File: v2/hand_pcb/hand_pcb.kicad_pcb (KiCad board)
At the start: 2 copper layers, 70 x 96.4 mm, 72 parts, among them J1 Screw_Terminal_01x10, J10 8P8C, J2 Conn_01x08, J3 Conn_01x08, J4 Conn_01x02, J5 Conn_01x02, J6 Conn_01x08, J7 Conn_01x03, J9 Conn_02x02_Top_Bottom, M1 Motor_Servo_FB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

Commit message: Doing some things
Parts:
- removed R26, R27, R28, R29: 0R, Resistor_THT:R_Axial_DIN0207_L6.3mm_D2.5mm_P10.16mm_Horizontal
- D1, D2, D3, D4, D5: value 1N5819 -> SB5100-T; footprint Diode_THT:D_DO-41_SOD81_P10.16mm_Horizontal -> Diode_THT:D_DO-201AD_P12.70mm_Horizontal
- U4, U5: value ADS7830 -> ~; footprint Package_SO:TSSOP-16_4.4x5mm_P0.65mm -> Package_DFN_QFN:WQFN-16-1EP_3x3mm_P0.5mm_EP1.68x1.68mm
- moved R7 169.2 mm to (26.8, 41.3), turned to 0 degrees
- moved R6 156.0 mm to (26.8, 37.3), turned to 0 degrees
- moved R5 143.1 mm to (26.8, 33.2), turned to 0 degrees
- moved H4 135.3 mm to (70.8, 66.1)
- moved R2 132.8 mm to (26.8, 21.1), turned to 0 degrees
- moved H2 129.8 mm to (70.8, 50.2)
- moved R1 121.2 mm to (26.8, 17.0), turned to 0 degrees
- moved H3 84.7 mm to (70.8, 58.2)
- moved J6 72.5 mm to (100.0, 17.3)
- moved H1 67.6 mm to (70.8, 42.3)
- moved R25 67.2 mm to (26.8, 81.8)
- moved U1 52.5 mm to (191.7, 81.4), turned to 90 degrees
- moved U5 41.4 mm to (210.8, 78.0), turned to 0 degrees
- moved J5 40.3 mm to (148.4, 114.8)
- moved C1 38.8 mm to (87.9, 62.5)
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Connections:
- R22 pad 1: Net-(U4-A0) -> Net-(U4-DECAP)
- R22 pad 2: +5V -> Net-(U4-ADDR)
- R23 pad 1: Net-(U4-A0) -> Net-(U4-ADDR)
- R24 pad 1: GND -> Net-(U5-DECAP)
- R24 pad 2: Net-(U4-A1) -> Net-(U5-ADDR)
- R25 pad 1: +5V -> Net-(U5-ADDR)
- R25 pad 2: Net-(U4-A1) -> GND
- U4 pad 1: SERVO_FB_8 -> SERVO_FB_6
- U4 pad 11: GND -> Net-(U4-ADDR)
- U4 pad 12: Net-(U4-A0) -> unconnected-(U4-ALERT-Pad12)
- U4 pad 13: Net-(U4-A1) -> SCL
- U4 pad 14: SCL -> SDA
- U4 pad 15: SDA -> SERVO_FB_8
- U4 pad 16: +5V -> SERVO_FB_7
- U4 pad 2: SERVO_FB_7 -> SERVO_FB_5
- U4 pad 3: SERVO_FB_6 -> SERVO_FB_4
- U4 pad 4: SERVO_FB_5 -> SERVO_FB_3
- U4 pad 5: SERVO_FB_4 -> SERVO_FB_2
- U4 pad 6: SERVO_FB_3 -> SERVO_FB_1
- U4 pad 7: SERVO_FB_2 -> +5V
- U4 pad 8: SERVO_FB_1 -> Net-(U4-DECAP)
- U5 pad 1: SERVO_FB_10 -> unconnected-(U5-AIN2-Pad1)
- U5 pad 11: GND -> Net-(U5-ADDR)
- U5 pad 12: Net-(U5-A0) -> unconnected-(U5-ALERT-Pad12)
- U5 pad 13: Net-(U5-A1) -> SCL
- U5 pad 14: SCL -> SDA
- U5 pad 15: SDA -> SERVO_FB_10
- U5 pad 16: +5V -> SERVO_FB_9
- U5 pad 2: SERVO_FB_9 -> unconnected-(U5-AIN3-Pad2)
- U5 pad 7: unconnected-(U5-CH6-Pad7) -> +5V
- U5 pad 8: unconnected-(U5-CH7-Pad8) -> Net-(U5-DECAP)
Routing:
- net +12V: track 47.9 -> 0.00 mm
- net SERVO_FB_8: track 0.00 -> 39.2 mm
- net SERVO_FB_7: track 0.00 -> 32.0 mm
- net SERVO_FB_6: track 0.00 -> 25.8 mm
- net SERVO_FB_5: track 0.00 -> 19.3 mm
- net DSCL+: track 0.00 -> 18.0 mm
- net DSDA-: track 3.18 -> 19.8 mm
- net SERVO_FB_4: track 0.00 -> 12.9 mm
- net DSCL-: track 0.00 -> 12.1 mm
- net SERVO_FB_1: track 0.00 -> 10.7 mm
- net DSDA+: track 3.18 -> 10.6 mm
- net Net-(D3-A): track 24.1 -> 16.9 mm
- net Net-(D4-A): track 24.1 -> 17.0 mm
- net SERVO_FB_3: track 0.00 -> 6.42 mm
- net Net-(D2-A): track 24.2 -> 17.9 mm
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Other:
- board outline removed

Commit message: Doing more things
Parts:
- removed J2, J3, J6: Conn_01x08, Connector_PinHeader_2.54mm:PinHeader_1x08_P2.54mm_Vertical
- moved R10 190.5 mm to (206.0, 118.1), turned to 90 degrees
- moved R24 188.4 mm to (215.0, 87.1), turned to 90 degrees
- moved R25 188.3 mm to (215.0, 89.9), turned to -90 degrees
- moved R7 186.4 mm to (210.5, 73.2), turned to 90 degrees
- moved R8 175.7 mm to (197.0, 89.0), turned to -90 degrees
- moved R6 173.4 mm to (196.5, 73.2), turned to 90 degrees
- moved R9 171.8 mm to (194.0, 89.0), turned to -90 degrees
- moved R5 160.6 mm to (182.5, 72.7), turned to 90 degrees
- moved R4 159.3 mm to (160.0, 116.6), turned to 90 degrees
- moved R3 158.7 mm to (156.5, 116.6), turned to 90 degrees
- moved H2 156.2 mm to (213.0, 115.0)
- moved R2 150.8 mm to (168.5, 72.7), turned to 90 degrees
- moved H3 143.4 mm to (213.0, 39.0)
- moved R1 139.2 mm to (154.5, 72.6), turned to 90 degrees
- moved R11 134.7 mm to (156.5, 93.9), turned to -90 degrees
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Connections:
- J9 pad 3: +5V -> +12V
- J9 pad 4: +12V -> +5V
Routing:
- net +12V: track 0.00 -> 173.6 mm, vias 0 -> 9
- net SDA: track 0.00 -> 113.9 mm, vias 0 -> 4
- net SCL: track 0.00 -> 109.7 mm, vias 0 -> 5
- net Net-(U2-GPA4): track 0.00 -> 58.0 mm, vias 0 -> 6
- net Net-(J2-Pin_1): track 2.02 -> 57.3 mm
- net Net-(J2-Pin_2): track 2.56 -> 52.9 mm
- net Net-(U2-GPA3): track 0.00 -> 46.8 mm, vias 0 -> 2
- net Net-(J2-Pin_3): track 2.10 -> 45.9 mm
- net Net-(U2-GPA0): track 0.00 -> 38.0 mm, vias 0 -> 3
- net Net-(U2-GPA2): track 0.00 -> 36.3 mm, vias 0 -> 3
- net Net-(J2-Pin_4): track 2.64 -> 37.5 mm
- net LIMIT_SW_R: track 0.00 -> 31.8 mm
- net Net-(J3-Pin_5): track 0.00 -> 31.1 mm, vias 0 -> 3
- net +5V: track 0.00 -> 30.9 mm, vias 0 -> 3
- net Net-(J2-Pin_5): track 2.19 -> 32.5 mm
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- added copper zone on B.Cu, net +12V
- added copper zone on F.Cu, net +5V
- added copper zone on B.Cu, net GND
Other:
- board outline added: 70 x 85 mm
- board text added: "+"
- board text added: "-"
- board text added: "BOT-HOVEN"
- board text added: "DESIGNED BY"
- board text added: "GND"
- board text added: "HAND PCB"
- board text added: "J. PETERSEN"
- board text added: "SCL"
- board text added: "SDA"
- board text added: "VERSION 2"

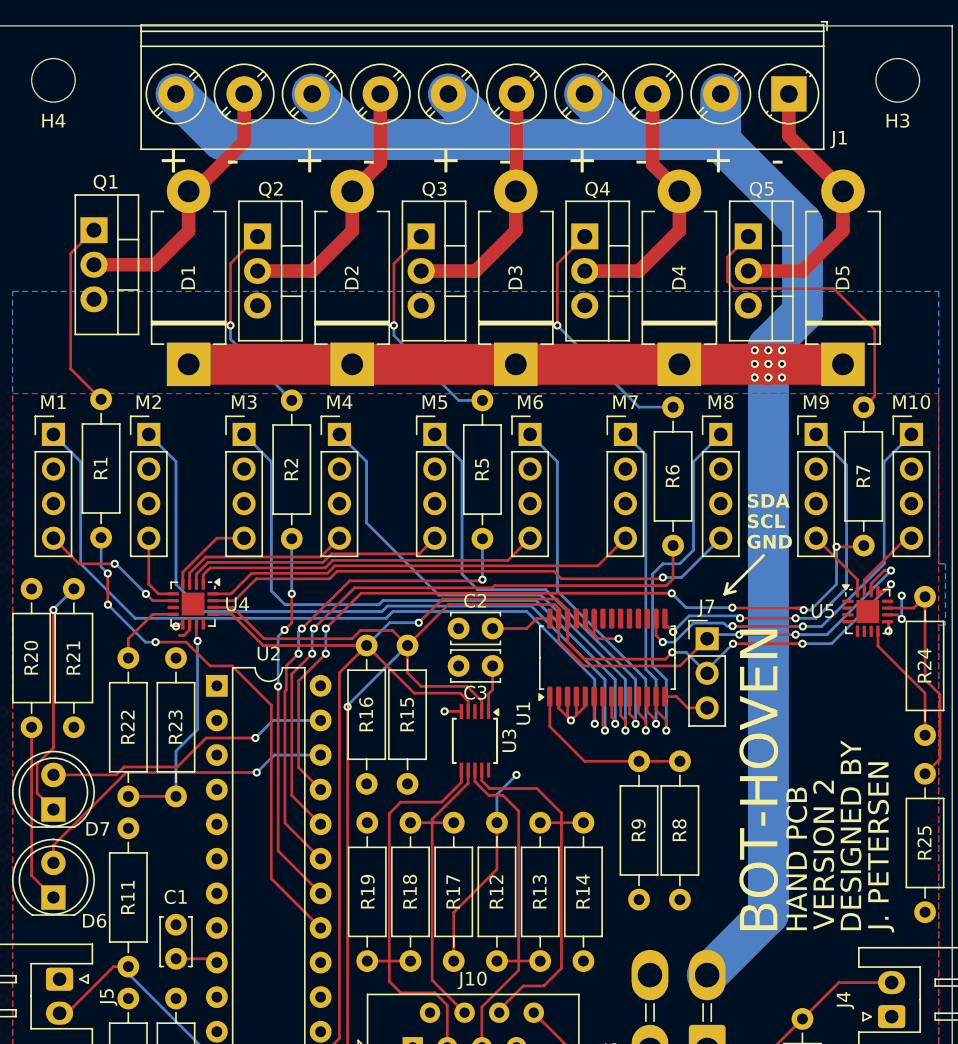
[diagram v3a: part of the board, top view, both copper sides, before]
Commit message: Version 2 As-Ordered commit
Minor changes to polish things up.
Version 2 is a major revision from the last revision, version 1. There are now 10 servo channels in addition to the 5 solenoid channels, and ADC feedback for those servos.
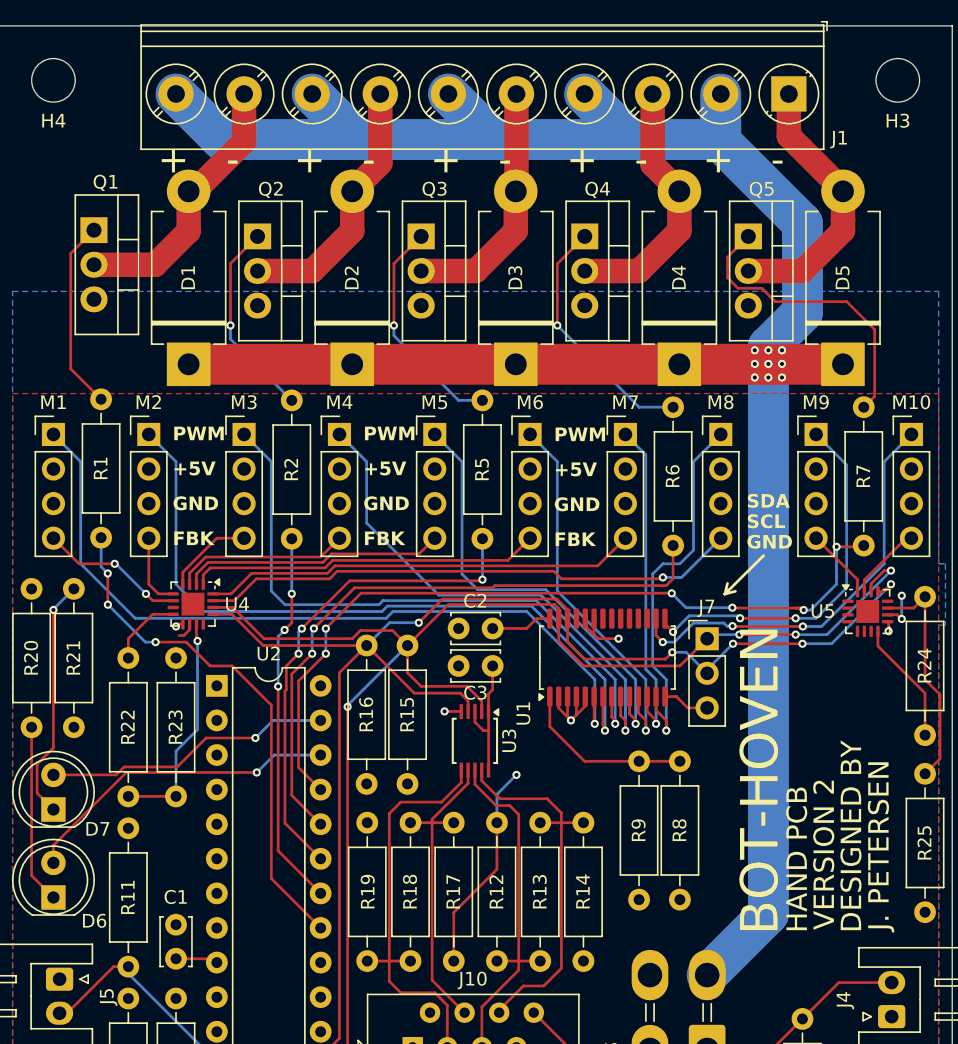
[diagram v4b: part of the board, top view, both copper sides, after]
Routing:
- net +5V: track 30.9 -> 37.3 mm
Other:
- board text added: "+5V"
- board text added: "FBK"
- board text added: "PWM"
